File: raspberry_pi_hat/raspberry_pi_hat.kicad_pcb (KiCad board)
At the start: 2 copper layers, 66.6 x 69.7 mm, 19 parts, among them IC2 LM3940IT, J1 LCD_screeen, J2 USB_C_Power, J3 GPIO, J4 GPIO, J5 Switches, J6 LED_status, U1 NRF24L01P

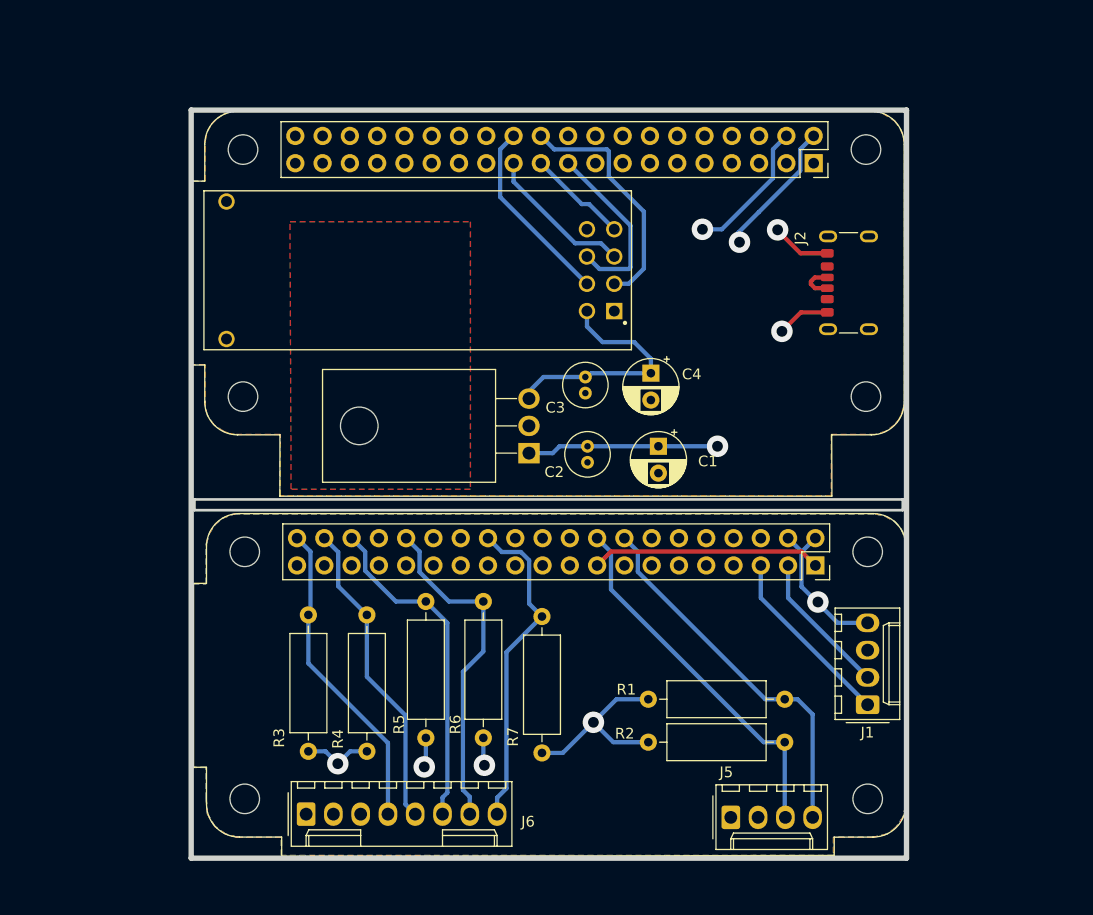
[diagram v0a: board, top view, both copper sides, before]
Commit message: Updated PCBs with professor changes to make first sample
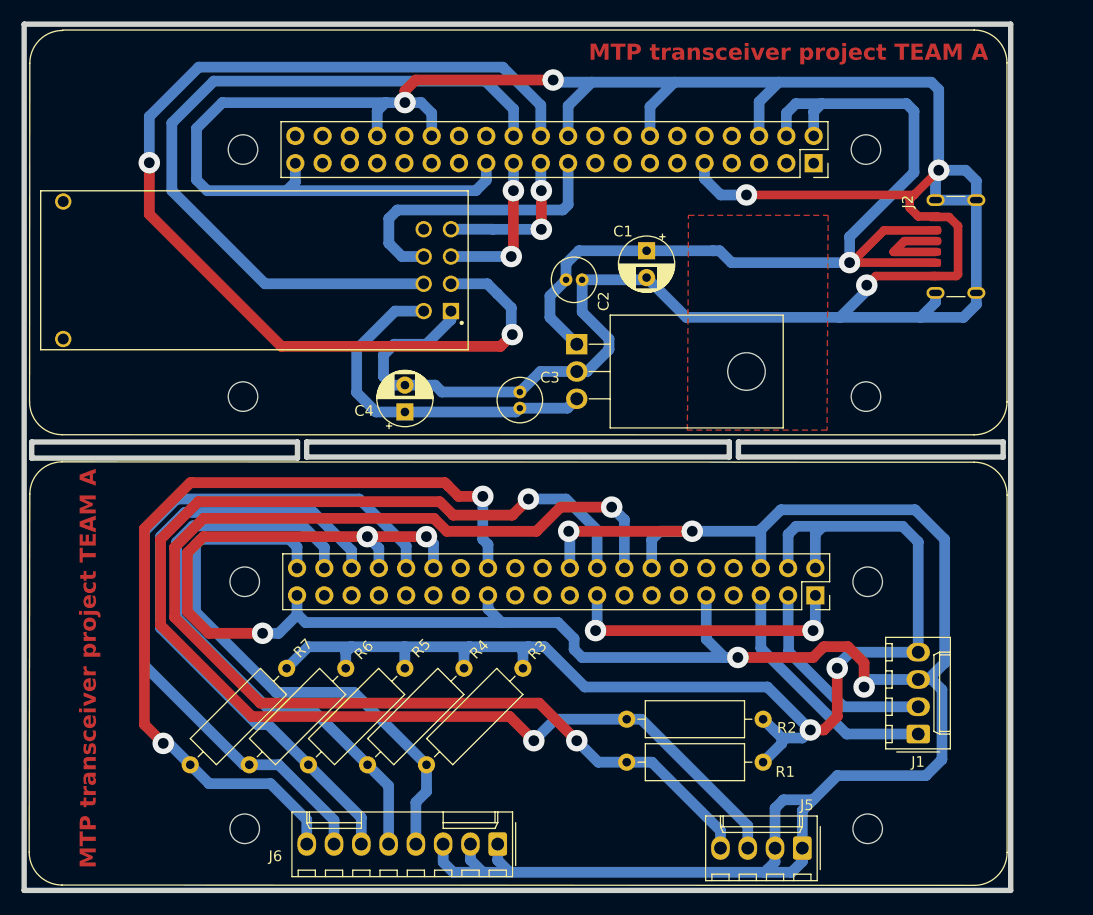
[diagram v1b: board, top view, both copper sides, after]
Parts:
- moved R7 25.0 mm to (109.0, 182.2), turned to -135 degrees
- moved C4 23.2 mm to (120.0, 158.3), turned to 90 degrees
- moved R3 21.4 mm to (131.0, 182.2), turned to -135 degrees
- moved C1 18.2 mm to (142.5, 143.3)
- moved J6 18.1 mm to (128.6, 198.5), turned to 180 degrees
- moved C2 15.6 mm to (135.0, 146.0), turned to 0 degrees
- moved U1 15.2 mm to (126.4, 137.2)
- moved R6 14.4 mm to (114.5, 182.2), turned to -135 degrees
- moved R1 12.2 mm to (153.3, 190.9), turned to 180 degrees
- moved R4 11.9 mm to (125.5, 182.2), turned to -135 degrees
- moved IC2 11.1 mm to (136.0, 152.0), turned to -90 degrees
- moved R2 10.9 mm to (153.3, 186.9), turned to 180 degrees
- moved J2 10.6 mm to (172.4, 142.9)
- moved J5 7.25 mm to (157.0, 198.9), turned to 180 degrees
- moved R5 6.77 mm to (120.0, 182.2), turned to -135 degrees
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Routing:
- net GND: track 10.5 -> 296.7 mm, vias 2 -> 5
- net GND1: track 0.00 -> 268.4 mm, vias 0 -> 7
- net /interface/GPIO24: track 34.4 -> 122.1 mm, vias 0 -> 2
- net /interface/GPIO23: track 35.0 -> 116.6 mm, vias 0 -> 2
- net CE: track 22.5 -> 100.0 mm, vias 0 -> 2
- net +5VA: track 44.0 -> 116.1 mm, vias 5 -> 2
- net CSN: track 17.6 -> 70.3 mm
- net /interface/GPIO7/SPI0.CE1: track 30.5 -> 80.0 mm, vias 0 -> 2
- net +5V: track 43.5 -> 88.1 mm, vias 3 -> 1
- net /interface/GPIO12/PWM0: track 31.6 -> 67.8 mm
- net /interface/GPIO16: track 31.2 -> 58.8 mm
- net /interface/GPIO20/PCM.DIN: track 29.2 -> 55.8 mm
- net /interface/GPIO21/PCM.DOUT: track 29.4 -> 53.4 mm
- net +3V3: track 22.7 -> 33.5 mm
- net /Transceiver/GPIO10/SPI0.MOSI: track 16.7 -> 27.1 mm
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- removed copper zone on F.Cu, net +5V
- removed copper zone on F.Cu, net +5VA
- removed copper zone on B.Cu, net GND
- removed copper zone on B.Cu, net GND1
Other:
- board size 66.6 x 69.7 mm -> 91.9 x 80.6 mm
- board text added: "MTP transceiver project TEAM A"
